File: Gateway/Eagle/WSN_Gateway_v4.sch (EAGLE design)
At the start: 15 parts, among them J1 5.5x2.1mm Barrel

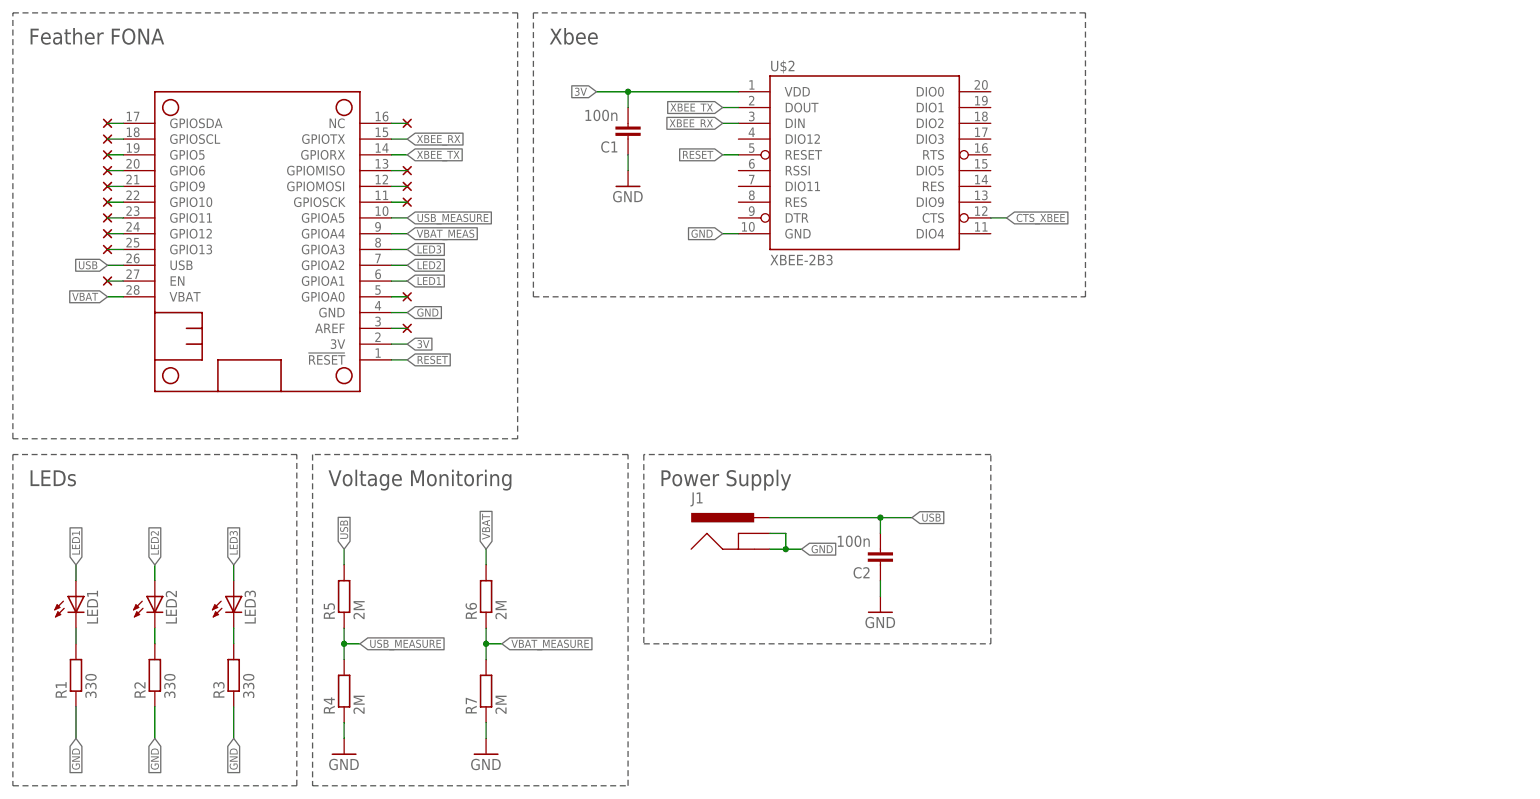
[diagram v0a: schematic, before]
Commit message: Added SMD pin headers to gateway board
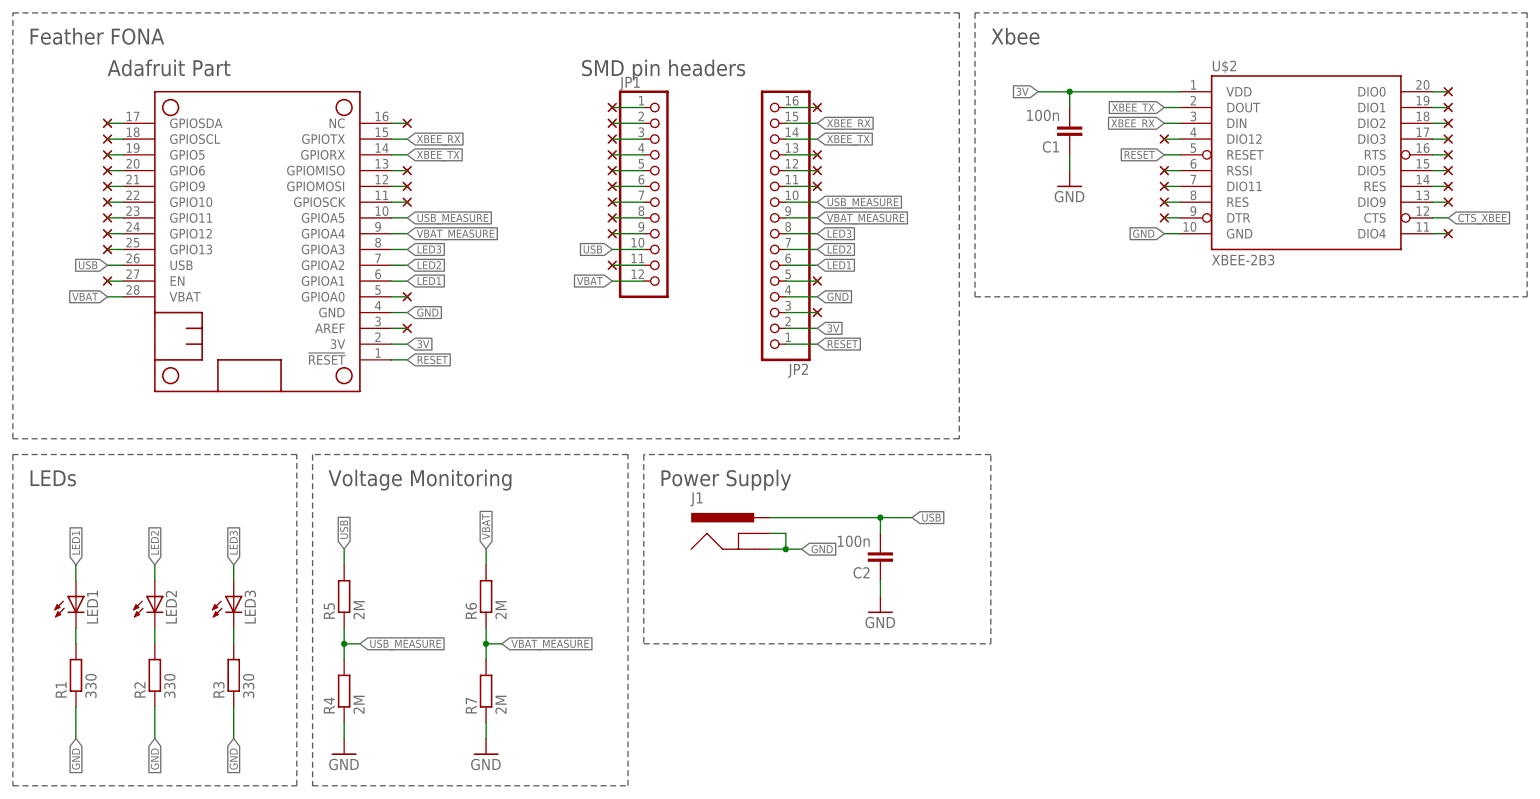
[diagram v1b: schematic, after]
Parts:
- added JP1: (no value), pinhead+:PINHD-1X121X12_SMT
- added JP2: (no value), pinhead+:PINHD-1X161X16_SMT
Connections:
- removed net VBAT_MEAS: MS1.GPIOA4
- new net N$19: JP1.1
- new net N$21: JP1.2
- new net N$22: JP1.3
- new net N$23: JP1.4
- new net N$24: JP1.5
- new net N$25: JP1.6
- new net N$26: JP1.7
- new net N$27: JP1.8
- new net N$28: JP1.9
- new net N$29: U$2.RSSI
- new net N$30: JP1.11
- new net N$31: U$2.DIO12
- new net N$32: JP2.16
- new net N$33: U$2.DIO11
- new net N$34: U$2.RES@8
- new net N$35: JP2.13
- new net N$36: JP2.12
- new net N$37: JP2.11
- new net N$38: U$2.DTR
- new net N$39: U$2.DIO0
- new net N$40: U$2.DIO1
- new net N$41: U$2.DIO2
- new net N$42: U$2.DIO3
- new net N$43: JP2.5
- new net N$44: U$2.RTS
- new net N$45: JP2.3
- new net N$46: U$2.DIO5
- new net N$47: U$2.RES@14
- new net N$48: U$2.DIO9
- new net N$49: U$2.DIO4
- net 3V: now also JP2.2
- net GND: now also JP2.4
- net LED1: now also JP2.6
- net LED2: now also JP2.7
- net LED3: now also JP2.8
- net RESET: now also JP2.1
- net USB: now also JP1.10
- net USB_MEASURE: now also JP2.10
- net VBAT: now also JP1.12
- net VBAT_MEASURE: now also JP2.9, MS1.GPIOA4
- net XBEE_RX: now also JP2.15
- net XBEE_TX: now also JP2.14
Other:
- note added: "Adafruit Part"
- note added: "SMD pin headers"
- moved on the sheet: C1, U$2
